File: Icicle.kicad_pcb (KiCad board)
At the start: 2 copper layers, 216 x 8 mm, 24 parts, among them P1 NeopixelStripPads, P2 NeopixelStripPads

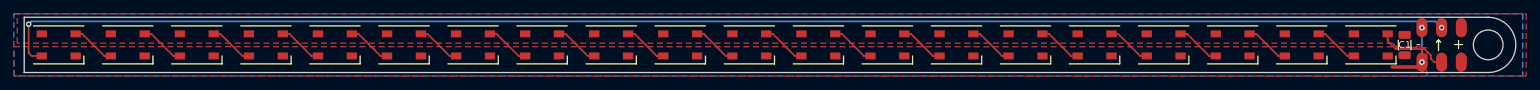
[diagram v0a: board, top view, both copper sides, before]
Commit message: Fixing DRC errors
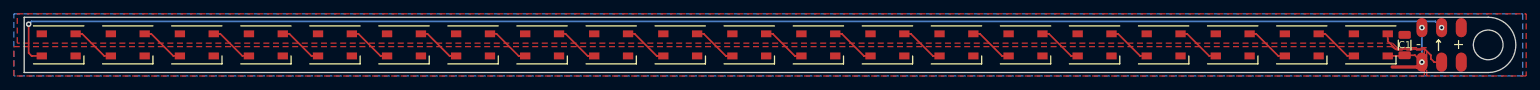
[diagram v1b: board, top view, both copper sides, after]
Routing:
- net GND: track 9.59 -> 15.0 mm
